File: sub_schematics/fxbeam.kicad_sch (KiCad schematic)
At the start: 14 parts

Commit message: Order prepare
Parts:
- FAN1: renamed from FAN_L1; JLCPCB Part # (none) -> C3169422; LCSC Part # C3169422 -> (none)
- FAN2: renamed from FAN_R1; JLCPCB Part # (none) -> C3169422; LCSC Part # C3169422 -> (none)
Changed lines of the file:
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@@
 		(in_pos_files yes)
 		(dnp no)
-		(property "Reference" "FAN_R1"
+		(property "Reference" "FAN2"
 			(at 118.11 337.312 0)
 			(show_name no)
@@
 		)
 		(property "Value" "F3311A7H121004E200"
-			(at 105.918 318.008 90)
+			(at 118.11 321.31 0)
+			(hide yes)
 			(show_name no)
 			(do_not_autoplace no)
@@
 		)
 		(property "MPN" "F3311A7H121004E200"
-			(at 113.284 353.568 0)
+			(at 113.03 331.47 0)
 			(hide yes)
 			(show_name no)
@@
 			)
 		)
-		(property "LCSC Part #" "C3169422"
+		(property "JLCPCB Part #" "C3169422"
 			(at 113.03 331.47 0)
 			(hide yes)
@@
 			(project "fw16_MCIO8i"
 				(path "/50f5fd03-67f8-43d1-8bfe-dca2cf908bf0/8477da45-41b5-48a1-9c5b-2402988eb1f4"
-					(reference "FAN_R1")
+					(reference "FAN2")
 					(unit 1)
 				)
@@
 		(in_pos_files yes)
 		(dnp no)
-		(property "Reference" "FAN_L1"
+		(property "Reference" "FAN1"
 			(at 118.11 313.182 0)
 			(show_name no)
@@
 		)
 		(property "Value" "F3311A7H121004E200"
-			(at 105.918 295.148 90)
+			(at 118.11 297.18 0)
+			(hide yes)
 			(show_name no)
 			(do_not_autoplace no)
@@
 		)
 		(property "MPN" "F3311A7H121004E200"
-			(at 113.284 329.438 0)
+			(at 113.03 307.34 0)
 			(hide yes)
 			(show_name no)
@@
 			)
 		)
-		(property "LCSC Part #" "C3169422"
+		(property "JLCPCB Part #" "C3169422"
 			(at 113.03 307.34 0)
 			(hide yes)
@@
 			(project "fw16_MCIO8i"
 				(path "/50f5fd03-67f8-43d1-8bfe-dca2cf908bf0/8477da45-41b5-48a1-9c5b-2402988eb1f4"
-					(reference "FAN_L1")
+					(reference "FAN1")
 					(unit 1)
 				)

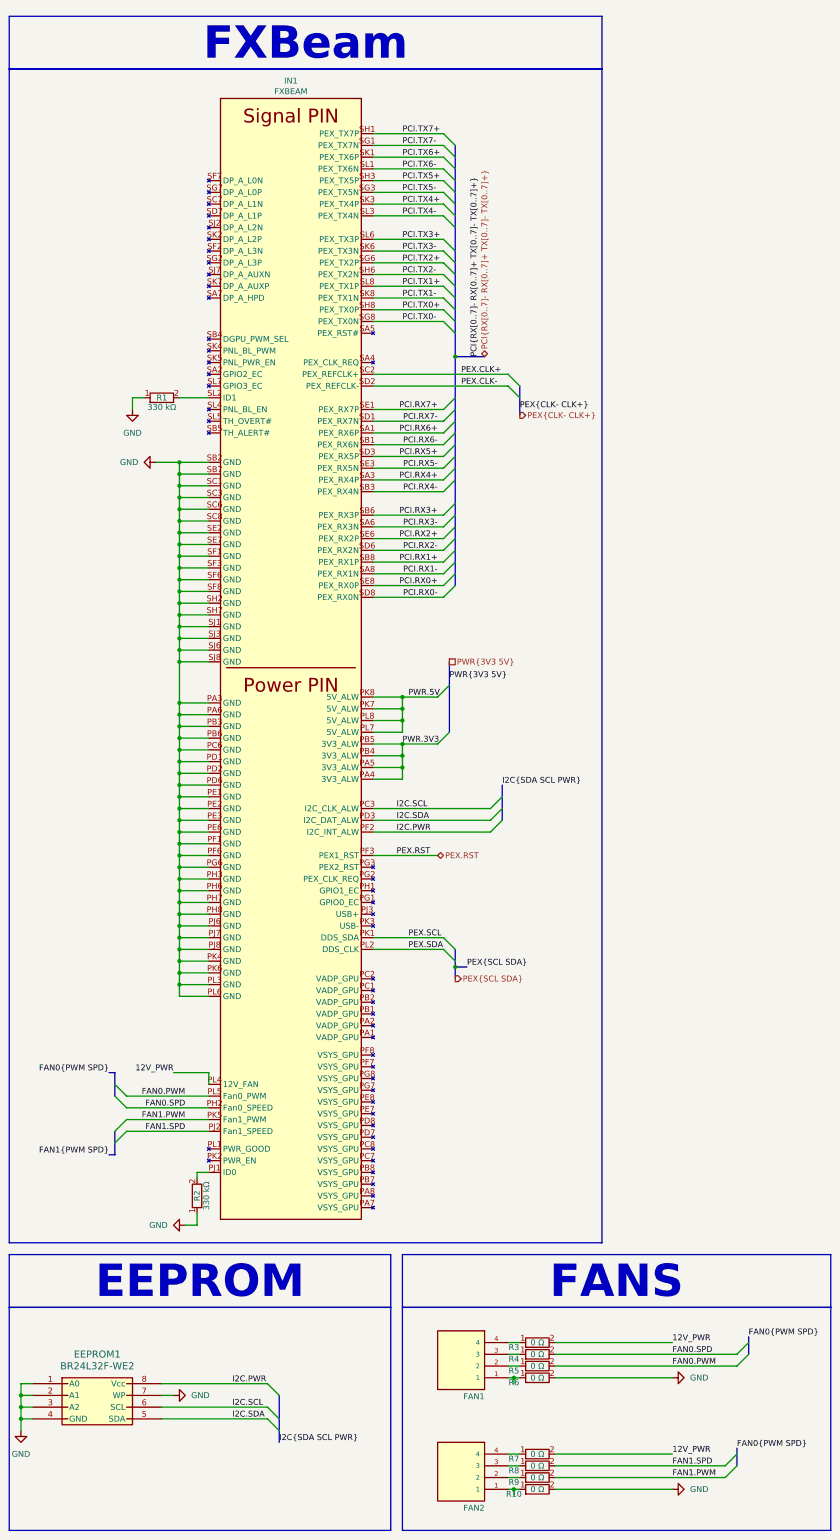
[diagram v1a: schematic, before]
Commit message: Reskew changed skematics
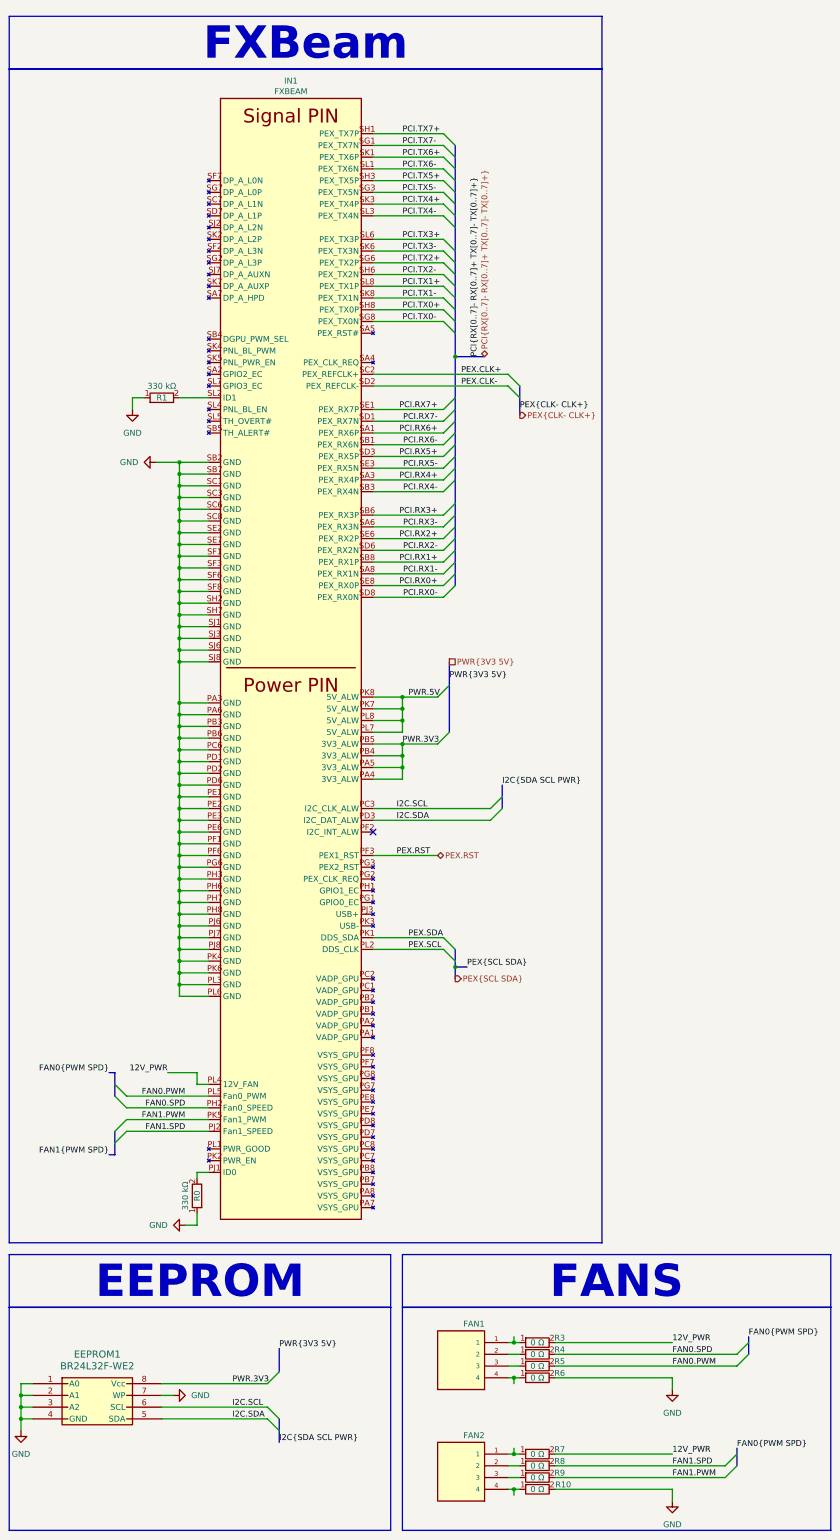
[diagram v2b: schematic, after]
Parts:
- R0: renamed from R2; value 0402_560112110088 -> 1206_R_560112132036; footprint WE_WRIS-RSKS:R_Wurth_WRIS-RSKS-0402 -> WE_WRIS-RSKS:R_Wurth_WRIS-RSKS-1206_W; symbol WE_WRIS-RSKS:0402_560112110088 -> WE_WRIS-RSKS:1206_R_560112132036; H (mm) 0.35 -> 0.6; JLCPCB Part # (none) -> C26798316; L (mm) 1.0 -> 3.1; MPN 560112110088 -> 560112132036; PRated (mW) 100.0 -> 250.0; Part Number 560112110088 -> 560112132036; Size 0402 -> 1206_R; VE (V) 50 -> 200; W (mm) 0.5 -> 1.6
- R1: value 0402_560112110088 -> 1206_R_560112132036; footprint WE_WRIS-RSKS:R_Wurth_WRIS-RSKS-0402 -> WE_WRIS-RSKS:R_Wurth_WRIS-RSKS-1206_W; symbol WE_WRIS-RSKS:0402_560112110088 -> WE_WRIS-RSKS:1206_R_560112132036; H (mm) 0.35 -> 0.6; JLCPCB Part # (none) -> C26798316; L (mm) 1.0 -> 3.1; MPN 560112110088 -> 560112132036; PRated (mW) 100.0 -> 250.0; Part Number 560112110088 -> 560112132036; Size 0402 -> 1206_R; VE (V) 50 -> 200; W (mm) 0.5 -> 1.6
- R10, R3, R4, R5, R6, R7, R8, R9: value 0402_560112110001 -> 1206_R_560112132007; footprint WE_WRIS-RSKS:R_Wurth_WRIS-RSKS-0402 -> WE_WRIS-RSKS:R_Wurth_WRIS-RSKS-1206_W; symbol WE_WRIS-RSKS:0402_560112110001 -> WE_WRIS-RSKS:1206_R_560112132007; H (mm) 0.35 -> 0.6; JLCPCB Part # C22463254 -> C25268462; L (mm) 1.0 -> 3.1; MPN 560112110001 -> 560112132007; PRated (mW) 62.5 -> 250.0; Part Number 560112110001 -> 560112132007; Size 0402 -> 1206_R; W (mm) 0.5 -> 1.6
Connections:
- net PEX.SCL: now also IN1.PL2 (DDS_CLK); no longer IN1.PK1 (DDS_SDA)
- net PEX.SDA: now also IN1.PK1 (DDS_SDA); no longer IN1.PL2 (DDS_CLK)
- net PWR.3V3: now also EEPROM1.8 (Vcc)
- net at R9.1: now also FAN2.3; no longer FAN2.2
- net at R3.1: now also FAN1.1; no longer FAN1.4
- net at R8.1: now also FAN2.2; no longer FAN2.3
- net at R4.1: now also FAN1.2; no longer FAN1.3
- net at R10.1: now also FAN2.4; no longer FAN2.1
- net at R6.1: now also FAN1.4; no longer FAN1.1
- net at R7.1: now also FAN2.1; no longer FAN2.4
- net at R5.1: now also FAN1.3; no longer FAN1.2
- net I2C.PWR: no longer names the net of IN1.PF2 (I2C_INT_ALW)
- net I2C.PWR: no longer EEPROM1.8 (Vcc)
- no-connect marks 0 -> 1

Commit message: updated kicad oot
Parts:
- renumbered R0 to ID0, R1 to ID1
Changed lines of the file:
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@@
 		(in_pos_files yes)
 		(dnp no)
-		(property "Reference" "R0"
+		(property "Reference" "ID0"
 			(at 55.88 270.51 0)
 			(show_name no)
@@
 			(project "fw16_MCIO8i"
 				(path "/50f5fd03-67f8-43d1-8bfe-dca2cf908bf0/8477da45-41b5-48a1-9c5b-2402988eb1f4"
-					(reference "R0")
+					(reference "ID0")
 					(unit 1)
 				)
@@
 		(in_pos_files yes)
 		(dnp no)
-		(property "Reference" "R1"
+		(property "Reference" "ID1"
 			(at 48.26 97.79 0)
 			(show_name no)
@@
 			(project "fw16_MCIO8i"
 				(path "/50f5fd03-67f8-43d1-8bfe-dca2cf908bf0/8477da45-41b5-48a1-9c5b-2402988eb1f4"
-					(reference "R1")
+					(reference "ID1")
 					(unit 1)
 				)

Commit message: schematics fixup
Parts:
- IN1: footprint expansion_bay:FXBeam -> (none)
